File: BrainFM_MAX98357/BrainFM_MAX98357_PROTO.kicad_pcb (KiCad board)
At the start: 2 copper layers, 14 parts, among them J1 USB_B_Micro, J2 Conn_01x07_Male, U2 MCP73831-2-OT, U3 TLV75801PDBV, U4 ESP32-WROOM-32

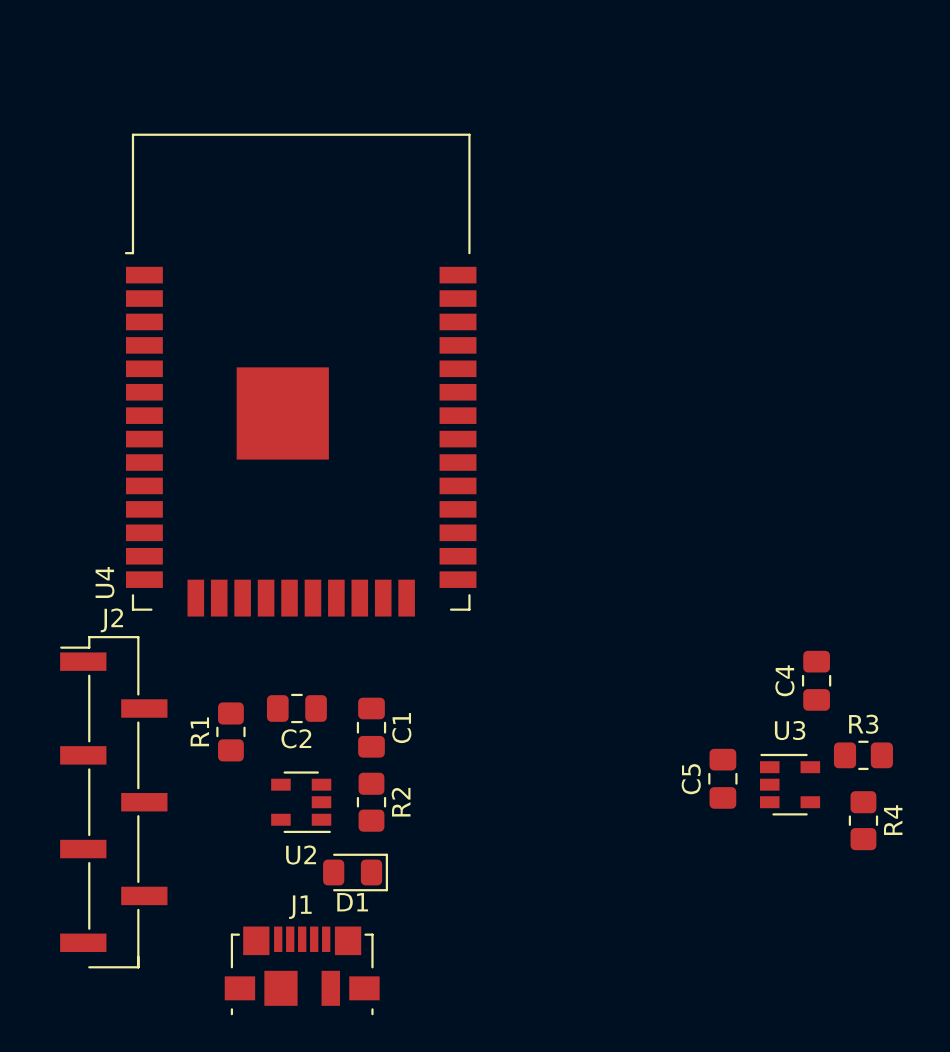
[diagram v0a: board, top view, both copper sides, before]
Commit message: start pcb layout on bottom layer
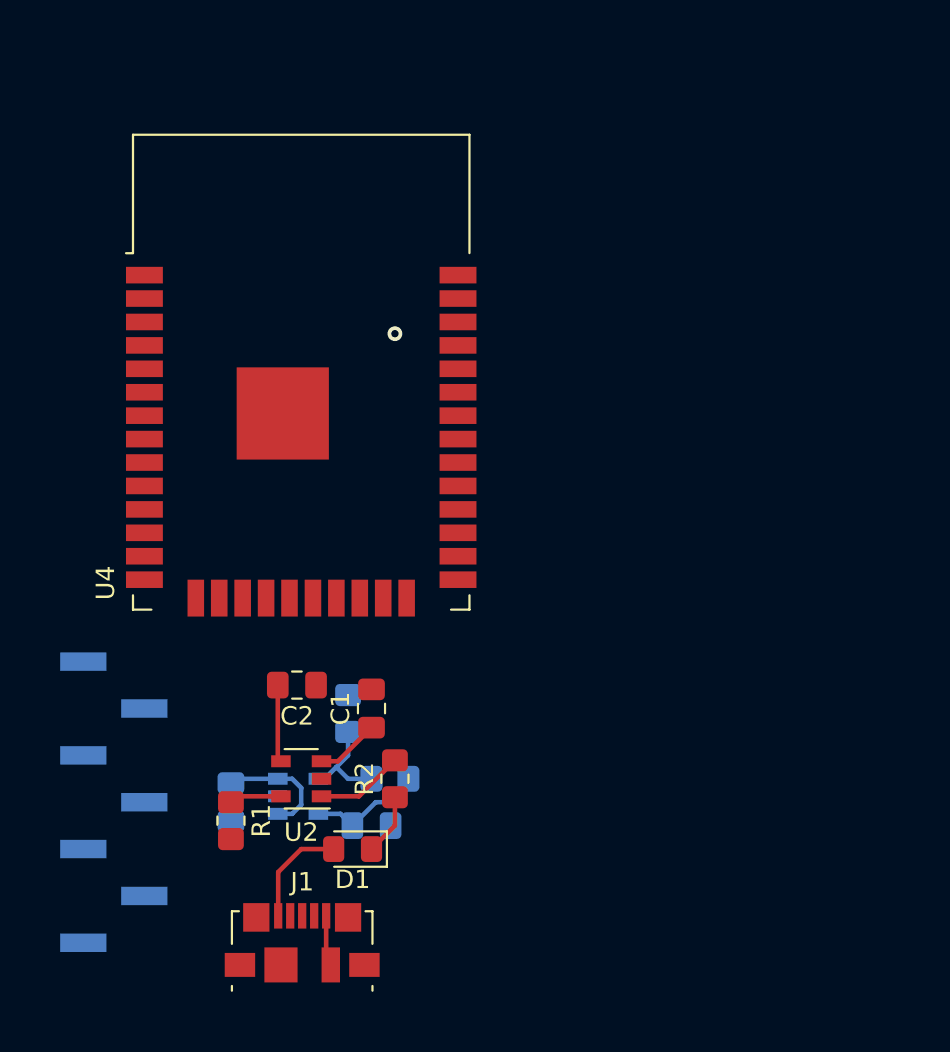
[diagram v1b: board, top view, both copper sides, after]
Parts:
- C4, C5, J2, R3, R4, U3: moved to B.Cu
- moved C4 32.4 mm to (141.0, 91.4), turned to 270 degrees
- moved R4 28.5 mm to (147.3, 86.6), turned to 90 degrees
- moved U3 26.7 mm to (144.6, 91.1)
- moved R3 25.7 mm to (149.6, 90.2), turned to 180 degrees
- moved C5 19.2 mm to (148.6, 92.7), turned to 0 degrees
- moved R1 4.81 mm to (141.0, 92.4), turned to 270 degrees
- moved R2 1.80 mm to (149.9, 90.2), turned to 90 degrees
- moved C2 1.27 mm to (144.5, 85.1)
- moved D1 1.27 mm to (147.6, 94.0)
- moved J1 1.27 mm to (144.8, 99.1)
- moved U2 1.27 mm to (144.8, 90.2)
- moved C1 1.04 mm to (148.6, 86.4), turned to 90 degrees
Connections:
- net Net-(U4-Pad3) renamed EN
- net Net-(U4-Pad34) renamed P_TX
- net Net-(U4-Pad35) renamed P_RX
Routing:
- net Net-(C2-Pad2): track 0.00 -> 10.1 mm
- net VCC: track 0.00 -> 6.50 mm
- net +3V3: track 0.00 -> 6.20 mm
- net Net-(R3-Pad2): track 0.00 -> 5.57 mm
- net Net-(R2-Pad2): track 0.00 -> 4.79 mm
- net Net-(C1-Pad1): track 0.00 -> 3.46 mm
- net Net-(D1-Pad1): track 0.00 -> 3.34 mm
- net Net-(R1-Pad1): track 0.00 -> 2.84 mm
- net -BATT: track 0.00 -> 2.76 mm
- net (no net): vias 0 -> 1

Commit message: backup before change to TC1262
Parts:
- added REF**: PinHeader_1x02_P2.54mm_Vertical, Connector_PinHeader_2.54mm:PinHeader_1x02_P2.54mm_Vertical, F.Cu at (157.0, 66.2)
- added REF**: PinHeader_1x02_P2.54mm_Vertical, Connector_PinHeader_2.54mm:PinHeader_1x02_P2.54mm_Vertical, F.Cu at (153.8, 87.2)
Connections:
- U4 pad 12: Net-(U4-Pad12) -> LRCK
- U4 pad 36: LRCK -> Net-(U4-Pad36)
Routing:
- net +3V3: track 6.20 -> 63.4 mm, vias 0 -> 1
- net -BATT: track 2.76 -> 29.8 mm
- net VCC: track 6.50 -> 25.4 mm
- net DATA: track 0.00 -> 17.3 mm, vias 0 -> 1
- net BCK: track 0.00 -> 13.4 mm, vias 0 -> 1
- net LRCK: track 0.38 -> 9.48 mm, vias 0 -> 1
- net Net-(C2-Pad2): track 10.1 -> 15.5 mm
- net P_TX: track 0.00 -> 4.07 mm
- net P_RX: track 0.00 -> 3.90 mm
- net (no net): vias 1 -> 0
- added copper zone on B.Cu, net -BATT
- added copper zone on F.Cu, net -BATT
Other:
- board outline added: 28.5 x 51.8 mm
